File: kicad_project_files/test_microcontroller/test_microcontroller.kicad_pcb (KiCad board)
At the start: 2 copper layers, 60 x 100 mm, 40 parts, among them J1 USB_C_Receptacle_USB2.0, SW1 SW_Push, SW2 SW_Push, SW3 SW_Push, SW4 SW_Push, SW5 SW_Push, SW6 SW_Push, SW7 SW_Push, SW8 SW_Push, SW9 SW_Push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

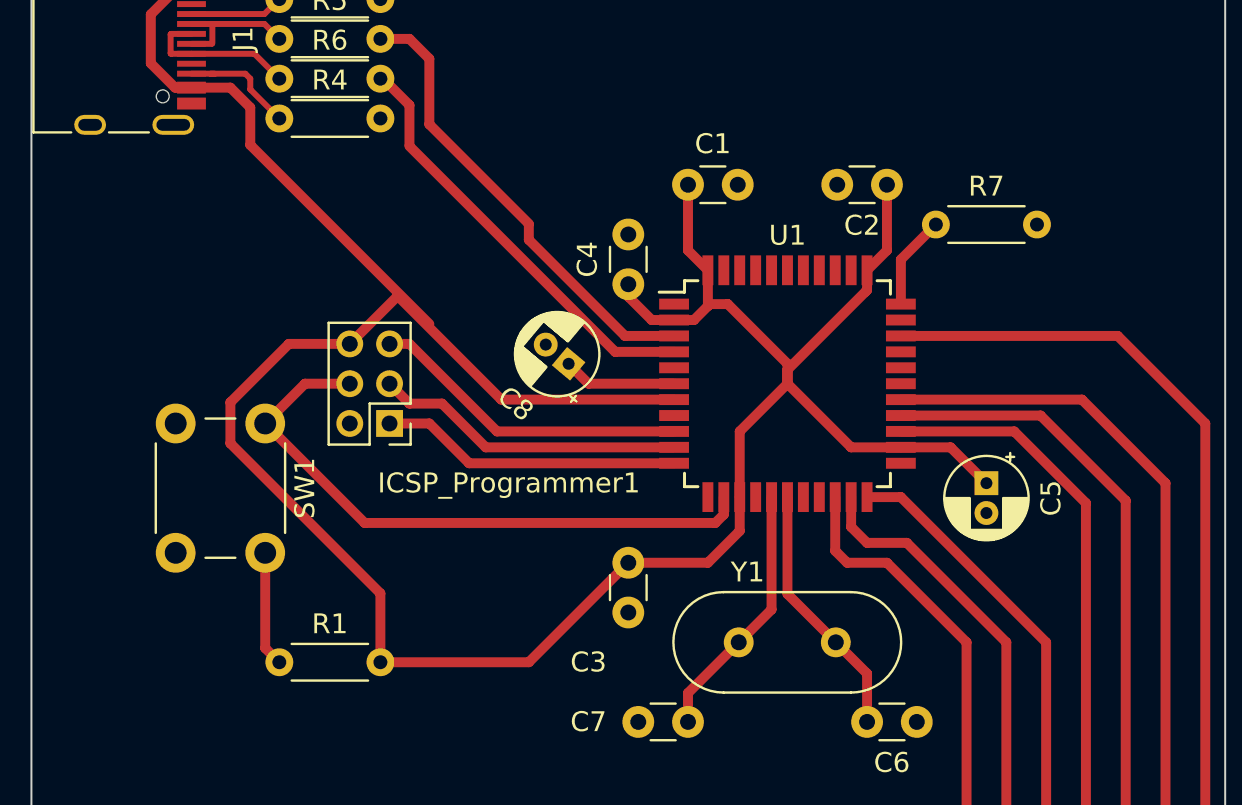
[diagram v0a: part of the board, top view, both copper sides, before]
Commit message: update to utmega8u2
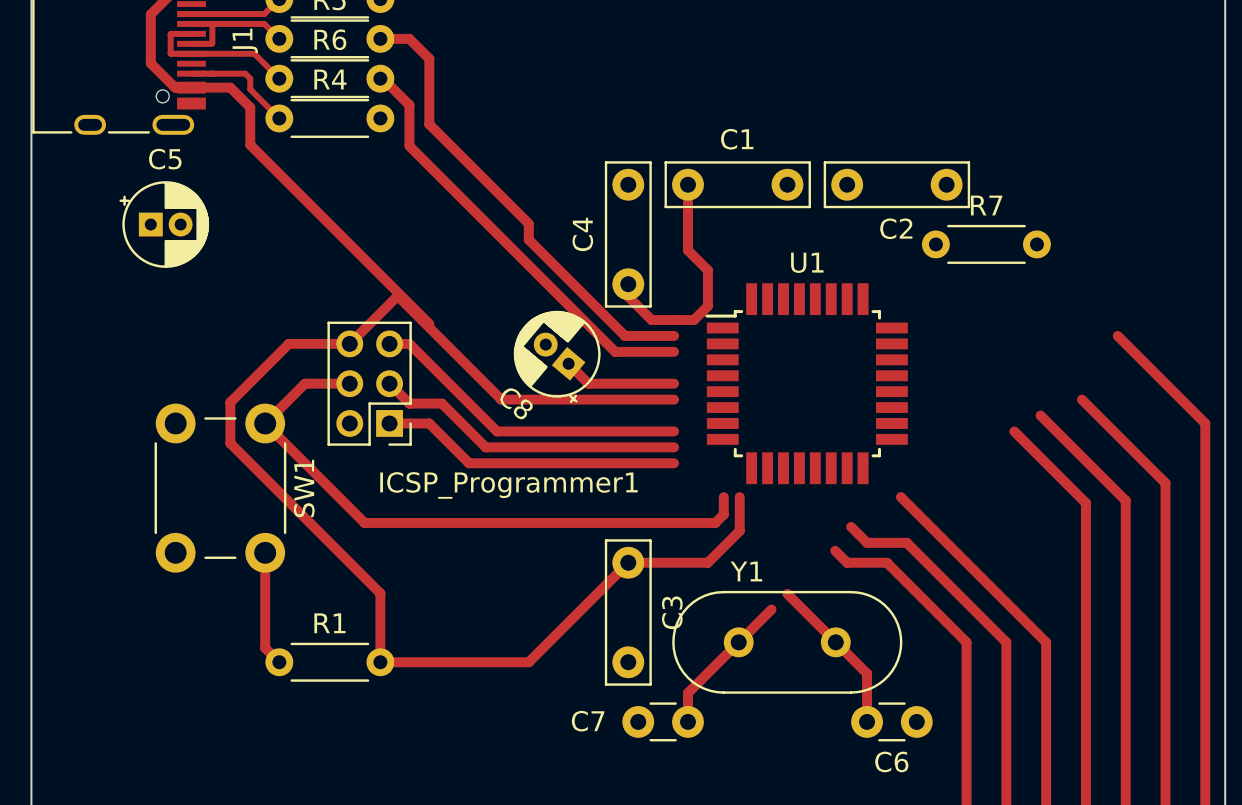
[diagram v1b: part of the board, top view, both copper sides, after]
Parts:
- C1, C2, C3, C4: footprint Capacitor_THT:C_Disc_D3.0mm_W1.6mm_P2.50mm -> Capacitor_THT:C_Rect_L7.0mm_W2.0mm_P5.00mm
- C5: value 1uf -> 10uf
- U1: value ATmega32U4-A -> ATmega8U2-A; footprint Package_QFP:TQFP-44_10x10mm_P0.8mm -> Package_QFP:TQFP-32_7x7mm_P0.8mm
- moved C5 44.0 mm to (35.0, 37.0), turned to 0 degrees
- moved C2 3.00 mm to (75.0, 35.0)
- moved R7 1.00 mm to (74.5, 38.0)
- moved U1 1.00 mm to (68.0, 45.0)
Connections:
- C1 pad 2: GNDREF -> GND
- C2 pad 2: GNDREF -> GND
- C3 pad 2: GNDREF -> GND
- C4 pad 2: GNDREF -> GND
- C5 pad 2: GNDREF -> GND
- D_CAPS1 pad 1: GNDREF -> GND
- ICSP_Programmer1 pad 2: GNDREF -> GND
- J1 pad A1: GNDREF -> GND
- J1 pad A12: GNDREF -> GND
- J1 pad B1: GNDREF -> GND
- J1 pad B12: GNDREF -> GND
- R2 pad 2: GNDREF -> GND
- R3 pad 2: GNDREF -> GND
- R4 pad 2: GNDREF -> GND
- SW1 pad 2: GNDREF -> GND
- U1 pad 1: unconnected-(U1-Pad1) -> Net-(C6-Pad2)
- U1 pad 10: MOSI -> unconnected-(U1-Pad10)
- U1 pad 11: MISO -> unconnected-(U1-Pad11)
- U1 pad 13: RESET -> Net-(R7-Pad1)
- U1 pad 14: VCC -> unconnected-(U1-Pad14)
- U1 pad 15: GNDREF -> SCLK
- U1 pad 16: Net-(C7-Pad2) -> MOSI
- U1 pad 17: Net-(C6-Pad2) -> MISO
- U1 pad 18: unconnected-(U1-Pad18) -> CAPS
- U1 pad 19: unconnected-(U1-Pad19) -> COL1
- U1 pad 2: VCC -> Net-(C7-Pad2)
- U1 pad 20: COL1 -> COL2
- U1 pad 21: COL2 -> COL3
- U1 pad 22: COL3 -> unconnected-(U1-Pad22)
- U1 pad 23: GNDREF -> unconnected-(U1-Pad23)
- U1 pad 24: VCC -> RESET
- U1 pad 25: ROW1 -> ROW3
- U1 pad 27: ROW3 -> Net-(C8-Pad1)
- U1 pad 28: unconnected-(U1-Pad28) -> GND
- U1 pad 29: unconnected-(U1-Pad29) -> D+
- U1 pad 3: D- -> GND
- U1 pad 30: unconnected-(U1-Pad30) -> D-
- U1 pad 31: CAPS -> VCC
- U1 pad 32: unconnected-(U1-Pad32) -> VCC
- U1 pad 4: D+ -> VCC
- U1 pad 5: GNDREF -> ROW1
- U1 pad 6: Net-(C8-Pad1) -> unconnected-(U1-Pad6)
- U1 pad 7: VCC -> unconnected-(U1-Pad7)
- U1 pad 9: SCLK -> unconnected-(U1-Pad9)
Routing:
- net VCC: track 139.9 -> 102.8 mm
- net CAPS: track 177.7 -> 166.8 mm
- net ROW3: track 130.7 -> 121.6 mm
- net ROW2: track 111.8 -> 104.8 mm
- net ROW1: track 96.0 -> 90.3 mm
- net Net-(C7-Pad2): track 13.0 -> 7.39 mm
- net Net-(C6-Pad2): track 13.0 -> 8.09 mm
- net Net-(R7-Pad1): track 4.73 -> 0.00 mm
- net COL1: track 68.8 -> 66.1 mm
- net COL3: track 46.5 -> 44.8 mm
- net COL2: track 55.7 -> 54.2 mm
- added copper zone on F.Cu, net GND
- removed copper zone on F.Cu, net GNDREF

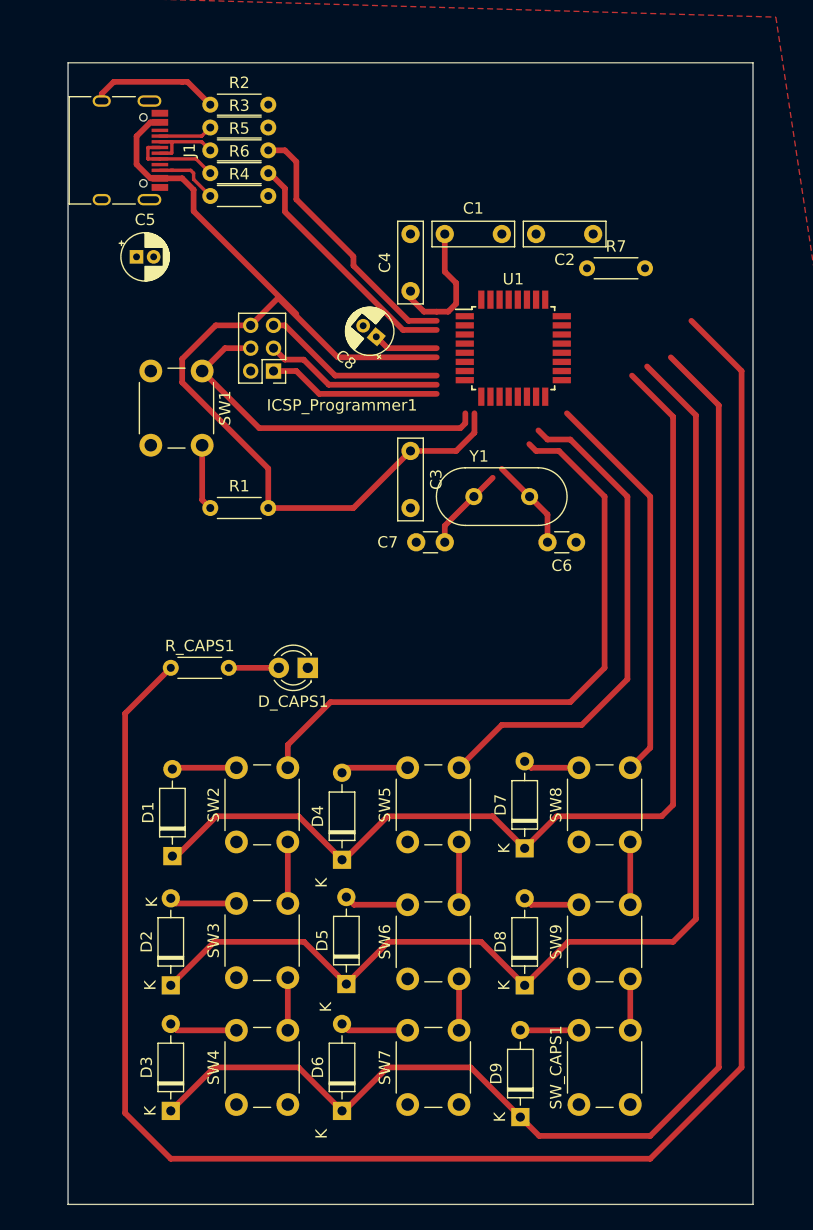
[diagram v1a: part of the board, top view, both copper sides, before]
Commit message: update schematic
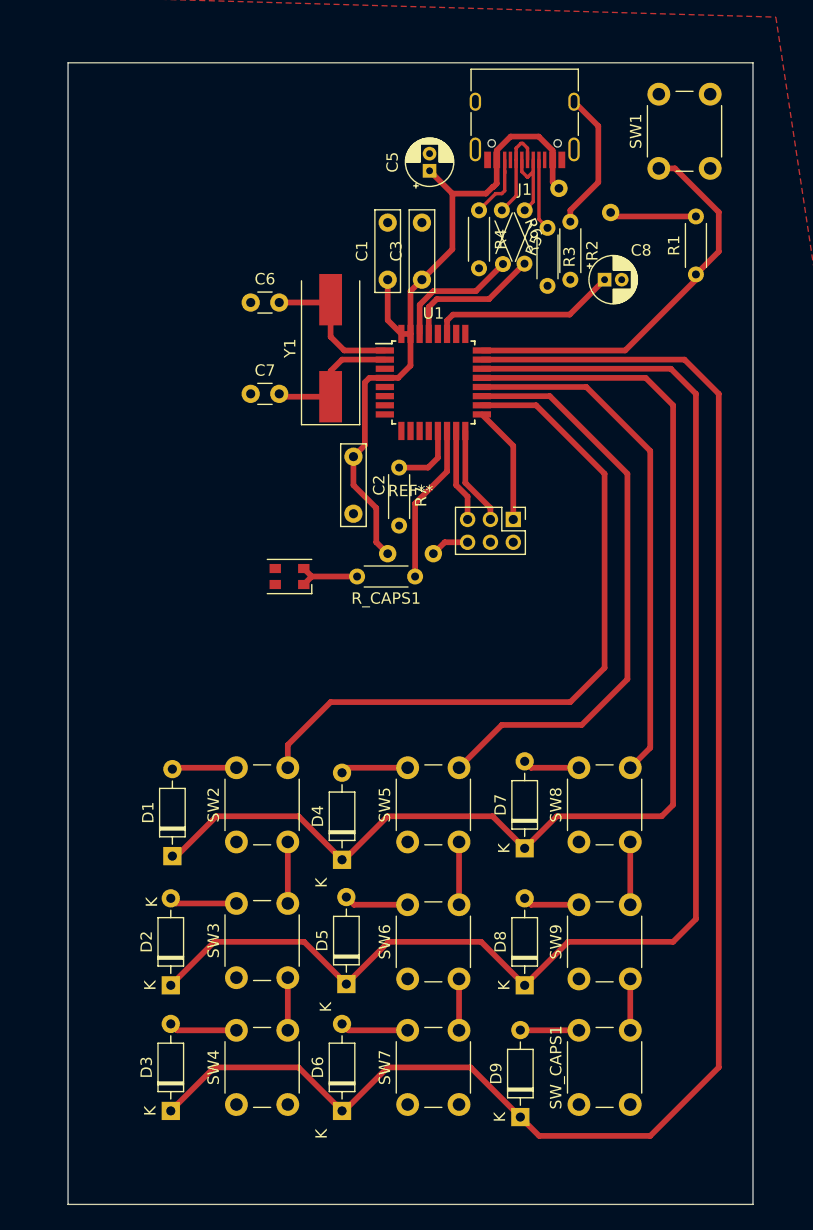
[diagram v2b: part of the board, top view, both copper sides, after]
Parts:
- removed C4: 0.1uf, Capacitor_THT:C_Rect_L7.0mm_W2.0mm_P5.00mm
- added REF**: Jumper_THT, Liam_CustomFootprints:Jumper_THT, F.Cu at (75.9, 27.3)
- added REF**: Jumper_THT, Liam_CustomFootprints:Jumper_THT, F.Cu at (59.0, 58.0)
- D_CAPS1: value LED -> CLA1A-WKW-CXAYB153; footprint LED_THT:LED_D3.0mm -> LED_SMD:LED_Cree-PLCC4_3.2x2.8mm_CCW
- Y1: footprint Crystal:Crystal_HC49-4H_Vertical -> Crystal:Crystal_SMD_HC49-SD
- moved R1 47.2 mm to (84.0, 38.5), turned to 90 degrees
- moved SW1 43.8 mm to (80.8, 29.2), turned to 90 degrees
- moved J1 36.1 mm to (69.0, 24.5), turned to 180 degrees
- moved C6 35.4 mm to (45.0, 41.0), turned to 0 degrees
- moved R2 33.2 mm to (73.0, 33.9), turned to -90 degrees
- moved R3 30.8 mm to (71.0, 34.5), turned to -90 degrees
- moved C2 28.7 mm to (54.0, 54.5), turned to -90 degrees
- moved R5 28.0 mm to (69.0, 32.9), turned to -112 degrees
- moved C5 26.8 mm to (60.7, 29.5), turned to 90 degrees
- moved R6 25.7 mm to (67.0, 32.9), turned to -67 degrees
- moved ICSP_Programmer1 24.7 mm to (68.0, 60.0), turned to -90 degrees
- moved R7 24.0 mm to (58.0, 55.5), turned to -90 degrees
- moved R4 23.6 mm to (65.0, 32.9), turned to -90 degrees
- moved R_CAPS1 22.8 mm to (59.4, 65.0), turned to 180 degrees
- moved C8 20.6 mm to (76.0, 39.0), turned to 0 degrees
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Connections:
- C6 pad 1: GNDREF -> GND
- C7 pad 1: GNDREF -> GND
- C8 pad 2: GNDREF -> GND
- D_CAPS1 pad 1: GND -> Net-(R_CAPS1-Pad2)
- D_CAPS1 pad 2: Net-(D_CAPS1-Pad2) -> Net-(R_CAPS1-Pad2)
- ICSP_Programmer1 pad 4: RESET -> unconnected-(ICSP_Programmer1-Pad4)
- R7 pad 2: GNDREF -> GND
- R_CAPS1 pad 2: Net-(D_CAPS1-Pad2) -> Net-(R_CAPS1-Pad2)
- U1 pad 14: unconnected-(U1-Pad14) -> CAPS
- U1 pad 18: CAPS -> COL1
- U1 pad 19: COL1 -> COL2
- U1 pad 20: COL2 -> COL3
- U1 pad 21: COL3 -> ROW1
- U1 pad 22: unconnected-(U1-Pad22) -> ROW2
- U1 pad 23: unconnected-(U1-Pad23) -> ROW3
- U1 pad 25: ROW3 -> unconnected-(U1-Pad25)
- U1 pad 26: ROW2 -> unconnected-(U1-Pad26)
- U1 pad 5: ROW1 -> unconnected-(U1-Pad5)
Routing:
- net CAPS: track 166.8 -> 13.9 mm
- net VCC: track 102.8 -> 74.4 mm
- net ROW3: track 121.6 -> 138.7 mm
- net ROW2: track 104.8 -> 120.3 mm
- net ROW1: track 90.3 -> 103.9 mm
- net D-: track 23.3 -> 11.3 mm
- net COL3: track 44.8 -> 55.5 mm
- net Net-(C8-Pad1): track 5.71 -> 16.5 mm
- net D+: track 21.6 -> 12.3 mm
- net SCLK: track 16.1 -> 8.41 mm
- net COL2: track 54.2 -> 61.5 mm
- net MOSI: track 15.6 -> 8.66 mm
- net COL1: track 66.1 -> 72.8 mm
- net Net-(R7-Pad1): track 0.00 -> 6.11 mm
- net Net-(R_CAPS1-Pad2): track 0.00 -> 5.95 mm
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
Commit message: fix pcb
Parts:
- moved C8 6.71 mm to (70.0, 42.0)
- moved R3 1.54 mm to (71.5, 33.0)
- moved R2 1.01 mm to (73.5, 33.0)
- moved C1 0.50 mm to (57.0, 38.5)
- moved C3 0.50 mm to (60.0, 38.5)
- moved R4 0.50 mm to (64.5, 32.9)
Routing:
- net Net-(C8-Pad1): track 16.5 -> 9.21 mm
- net Net-(J1-PadA5): track 6.27 -> 5.01 mm
- net Net-(J1-PadS1): track 12.4 -> 11.3 mm
- net VCC: track 74.4 -> 74.9 mm

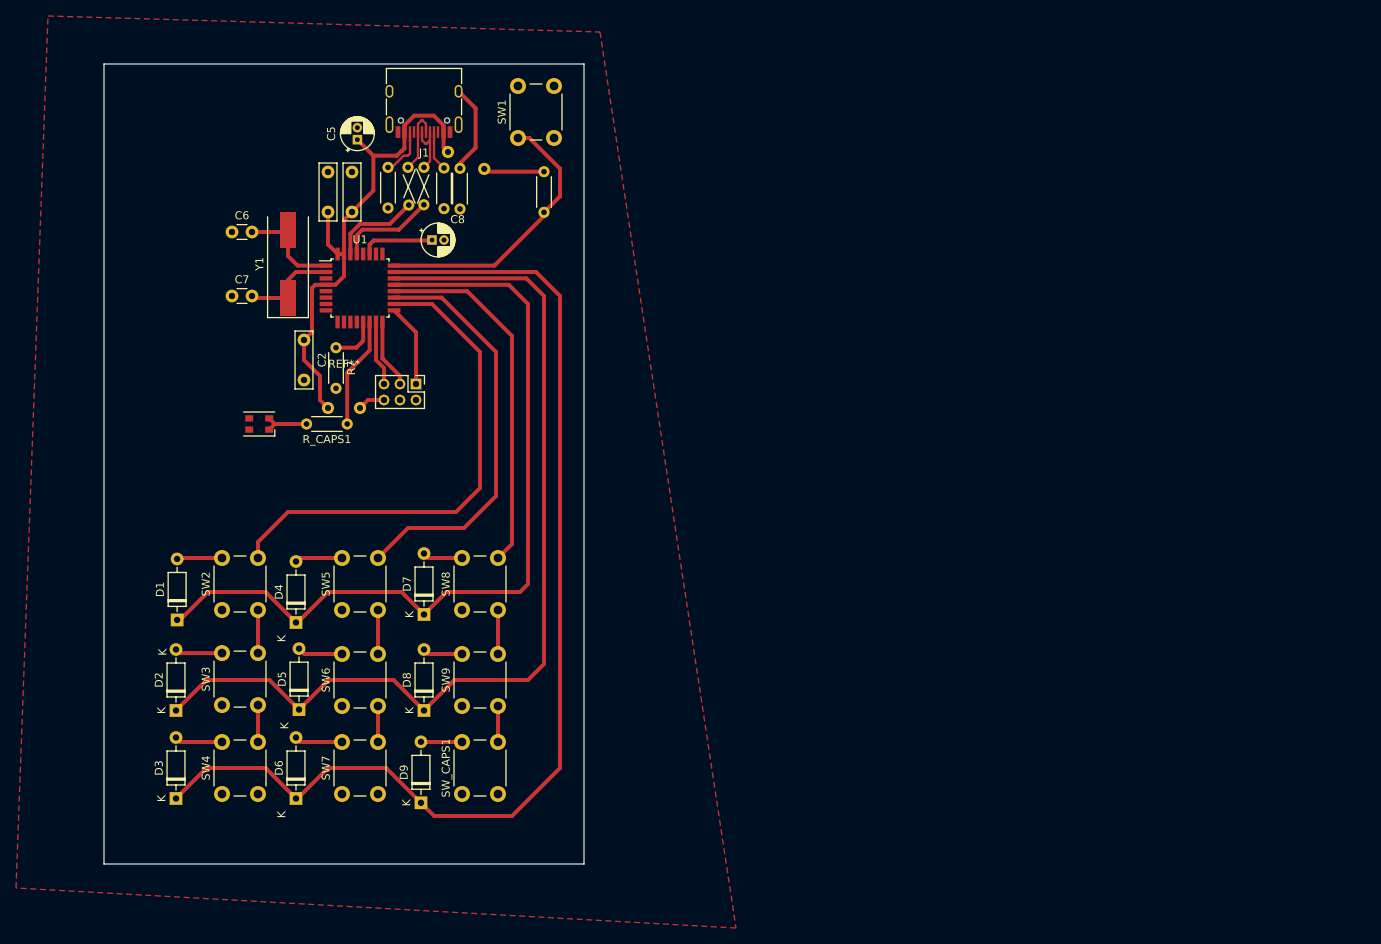
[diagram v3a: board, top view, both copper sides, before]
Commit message: make pcb smaller
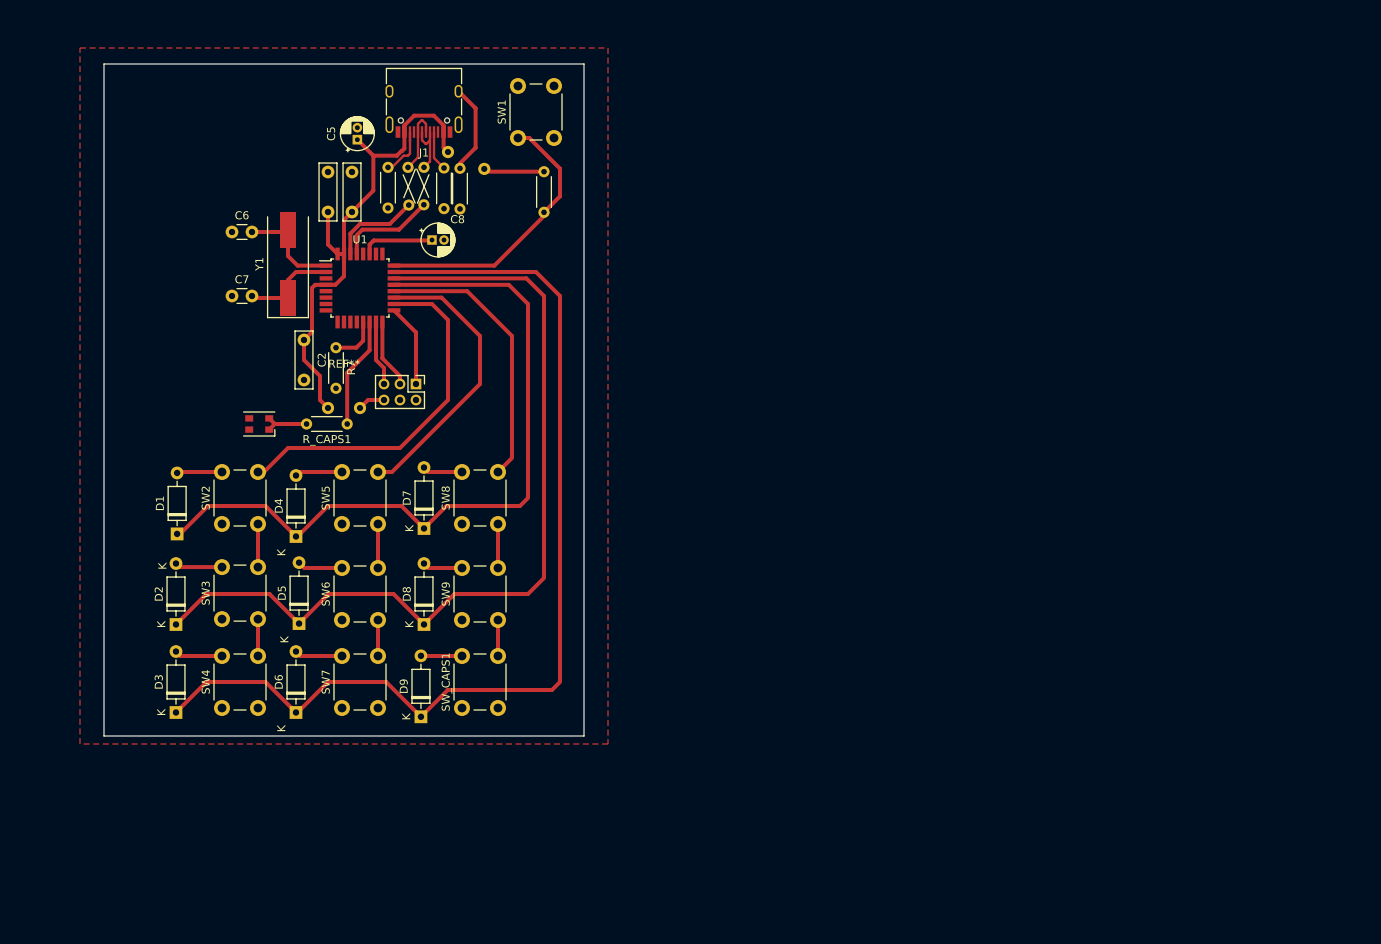
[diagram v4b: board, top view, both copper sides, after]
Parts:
- moved D1 10.8 mm to (38.1, 78.7)
- moved D2 10.8 mm to (38.0, 90.1)
- moved D3 10.8 mm to (38.0, 101.1)
- moved D4 10.8 mm to (53.0, 79.1)
- moved D5 10.8 mm to (53.4, 89.9)
- moved D6 10.8 mm to (53.0, 101.1)
- moved D7 10.8 mm to (69.0, 78.1)
- moved D8 10.8 mm to (69.0, 90.1)
- moved D9 10.8 mm to (68.6, 101.6)
- moved SW2 10.8 mm to (43.8, 77.5)
- moved SW3 10.8 mm to (43.8, 89.4)
- moved SW4 10.8 mm to (43.8, 100.5)
- moved SW5 10.8 mm to (58.8, 77.5)
- moved SW6 10.8 mm to (58.8, 89.5)
- moved SW7 10.8 mm to (58.8, 100.5)
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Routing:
- net COL1: track 72.8 -> 55.1 mm
- net COL2: track 61.5 -> 46.0 mm
- net ROW3: track 138.7 -> 126.3 mm
- net ROW2: track 120.3 -> 109.3 mm
- net ROW1: track 103.9 -> 92.9 mm
- net COL3: track 55.5 -> 44.5 mm
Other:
- board size 60 x 100 mm -> 60 x 84 mm

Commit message: update pcb
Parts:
- moved R_CAPS1 11.1 mm to (49.3, 60.5)
- moved D_CAPS1 9.53 mm to (40.0, 60.5)
- moved REF** 9.51 mm to (49.5, 58.5), turned to 90 degrees
- moved C2 7.07 mm to (47.0, 55.5), turned to 180 degrees
- moved D1 4.25 mm to (38.1, 74.5)
- moved D2 4.25 mm to (38.0, 85.8)
- moved D3 4.25 mm to (38.0, 96.8)
- moved D4 4.25 mm to (53.0, 74.8)
- moved D5 4.25 mm to (53.4, 85.7)
- moved D6 4.25 mm to (53.0, 96.8)
- moved D8 4.25 mm to (69.0, 85.8)
- moved D9 4.25 mm to (68.6, 97.3)
- moved SW2 4.25 mm to (43.8, 73.2)
- moved SW3 4.25 mm to (43.8, 85.1)
- moved SW4 4.25 mm to (43.8, 96.2)
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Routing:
- net RESET: track 34.9 -> 29.7 mm
- net CAPS: track 13.9 -> 18.4 mm
- net ROW3: track 126.3 -> 122.3 mm
- net ROW2: track 109.3 -> 105.3 mm
- net COL3: track 44.5 -> 40.5 mm
- net VCC: track 74.9 -> 78.4 mm
- net ROW1: track 92.9 -> 89.7 mm
- net COL2: track 46.0 -> 44.1 mm
- net COL1: track 55.1 -> 53.3 mm
- net Net-(R_CAPS1-Pad2): track 5.95 -> 4.19 mm
- net SCLK: track 8.41 -> 7.91 mm
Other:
- board size 60 x 84 mm -> 53 x 80 mm
